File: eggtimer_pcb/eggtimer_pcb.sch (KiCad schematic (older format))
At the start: 84 parts, among them J1 Conn_01x03, Q1 CPH3350-TL-W, Q10 2N7002P,215, Q2 CPH3350-TL-W, Q3 CPH3350-TL-W, Q4 CPH3350-TL-W, Q5 CPH3350-TL-W, Q6 CPH3350-TL-W, Q7 CPH3350-TL-W, Q8 CPH3350-TL-W, Q9 2N7002P,215, SW1 Rotary_Encoder_Switch, SW2 SW_Push, U1 BD70522GUL-E2, U2 STM32G051GxU, Y1 32.xxxk

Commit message: MORE LEDS
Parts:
- removed D10, D11, D12, D13, D14, D15, D16, D17, D18, D19, D2, D20, D21, D22, D23, D24, D25, D26, D27, D28, D29, D3, D30, D31, D32, D33, D34, D35, D36, D37, D4, D5, D6, D7, D8, D9: TLMS1000-GS08, LED_SMD:LED_0603_1608Metric_Pad1.05x0.95mm_HandSolder, symbol Device:LED
- removed Q1, Q2, Q3, Q4, Q5, Q6: CPH3350-TL-W, Package_TO_SOT_SMD:SOT-23_Handsoldering, symbol Device:Q_PMOS_GSD
- removed R1, R3, R5, R6, R7, R8: 200, Resistor_SMD:R_0603_1608Metric_Pad0.98x0.95mm_HandSolder, symbol Device:R_Small
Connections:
- net power_ctrl: now also U2.7 (PA1); no longer U2.8 (PA2)
- net power_on: no longer Q8.1 (G), Q9.3 (D), R2.1
- net led_c7: now reaches U2.15 (PB1)
- net led_a7: now reaches U2.17 (PC6)
- net led_a6: now reaches U2.22 (PA15)
- new net: Q8.1 (G), Q9.3 (D), R2.1
- new net led_c6: U2.8 (PA2)
- no-connect marks 6 -> 1
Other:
- moved on the sheet: BT1, BT2, BZ1, C1, C2, C3, C4, C5, C6, C7, C8, D1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

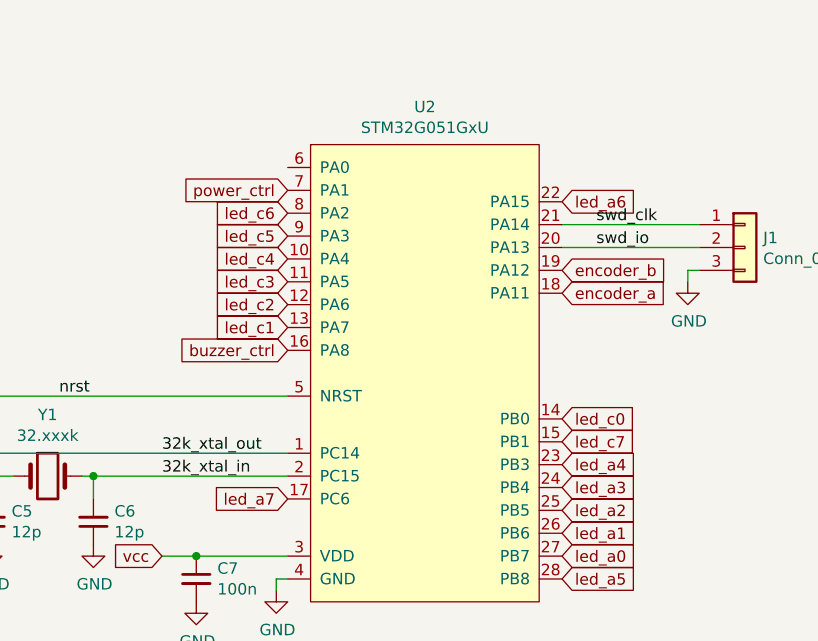
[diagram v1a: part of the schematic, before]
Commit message: Finalize rev2.1 pcb
make sure that schema is up to date with stmcubemx
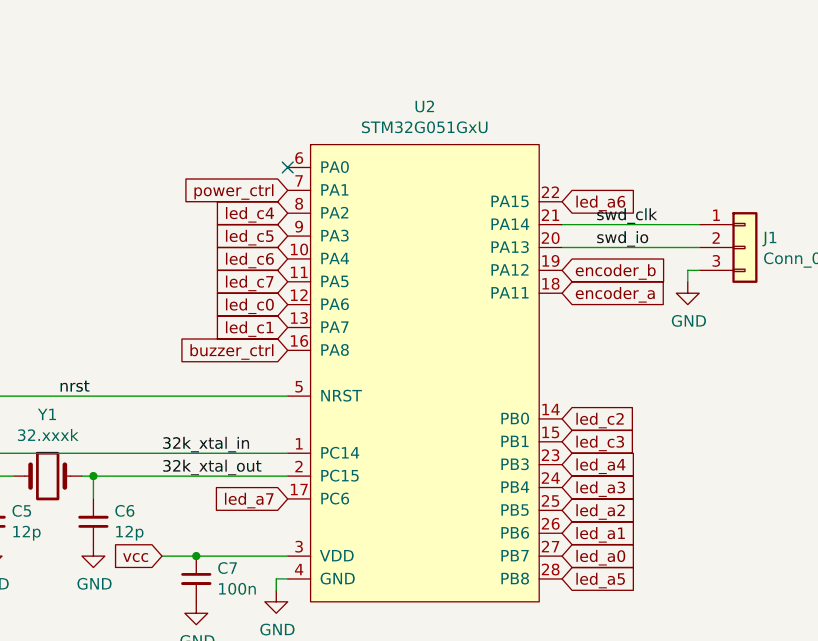
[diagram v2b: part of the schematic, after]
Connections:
- net 32k_xtal_in: now also C5.2, U2.1 (PC14), Y1.1; no longer C6.2, U2.2 (PC15), Y1.2
- net 32k_xtal_out: now also C6.2, U2.2 (PC15), Y1.2; no longer C5.2, U2.1 (PC14), Y1.1
- net led_c0: now also U2.12 (PA6); no longer U2.14 (PB0)
- net led_c2: now also U2.14 (PB0); no longer U2.12 (PA6)
- net led_c3: now also U2.15 (PB1); no longer U2.11 (PA5)
- net led_c4: now also U2.8 (PA2); no longer U2.10 (PA4)
- net led_c6: now also U2.10 (PA4); no longer U2.8 (PA2)
- net led_c7: now also U2.11 (PA5); no longer U2.15 (PB1)
- no-connect marks 1 -> 2
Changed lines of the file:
@@
 	1    0    0    -1
 $EndComp
+Text Label 7900 5100 0    50   ~ 0
+32k_xtal_out
 Text Label 7900 5000 0    50   ~ 0
-32k_xtal_out
-Text Label 7900 5100 0    50   ~ 0
 32k_xtal_in
 Text GLabel 9650 4300 2    50   Input ~ 0
@@
 	8450 5100 7600 5100
 Connection ~ 7600 5100
-Text GLabel 9650 4850 2    50   Input ~ 0
+Text GLabel 8450 4350 0    50   Input ~ 0
 led_c0
 Text GLabel 8450 4050 0    50   Input ~ 0
 led_c5
-Text GLabel 8450 4150 0    50   Input ~ 0
+Text GLabel 8450 3950 0    50   Input ~ 0
 led_c4
-Text GLabel 8450 4250 0    50   Input ~ 0
+Text GLabel 9650 4950 2    50   Input ~ 0
 led_c3
-Text GLabel 8450 4350 0    50   Input ~ 0
+Text GLabel 9650 4850 2    50   Input ~ 0
 led_c2
 Text GLabel 8450 4450 0    50   Input ~ 0
@@
 Text GLabel 2800 1250 0    50   Input ~ 0
 led_a0
-Text GLabel 9650 4950 2    50   Input ~ 0
+Text GLabel 8450 4250 0    50   Input ~ 0
 led_c7
-Text GLabel 8450 3950 0    50   Input ~ 0
+Text GLabel 8450 4150 0    50   Input ~ 0
 led_c6
 Text GLabel 9650 3900 2    50   Input ~ 0
@@
 Text GLabel 8450 5200 0    50   Input ~ 0
 led_a7
+NoConn ~ 8450 3750
 $EndSCHEMATC
